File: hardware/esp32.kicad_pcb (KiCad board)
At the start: 4 copper layers, 60 x 40 mm, 86 parts, among them J101 USB-C-2, P101 EXT_HEADER, P201 CON-SENSOR2, P202 CON-SENSOR2, P203 CON-SENSOR2, P204 CON-SENSOR2, P205 CON-SENSOR2, P206 CON-SENSOR2, Q101 BC817, Q102 BC817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

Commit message: fix values
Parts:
- R108, R109: value 1k -> 2k2
- R110: value 470 -> 220

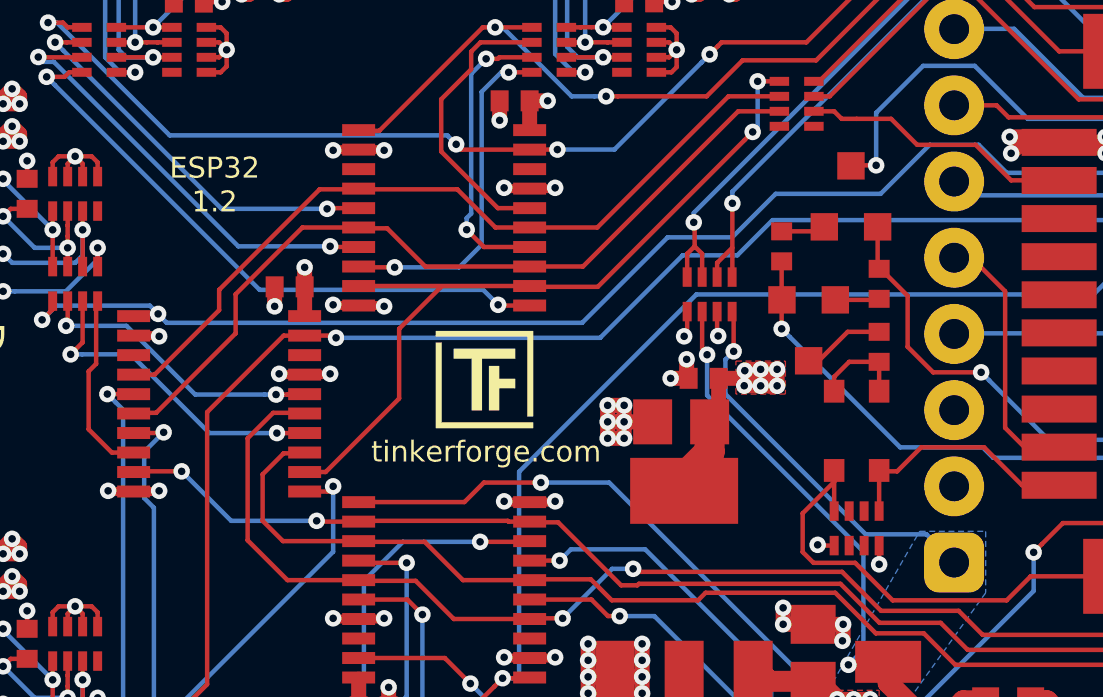
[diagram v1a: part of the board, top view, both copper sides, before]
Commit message: hardware version 1.3
 * fix reset logic
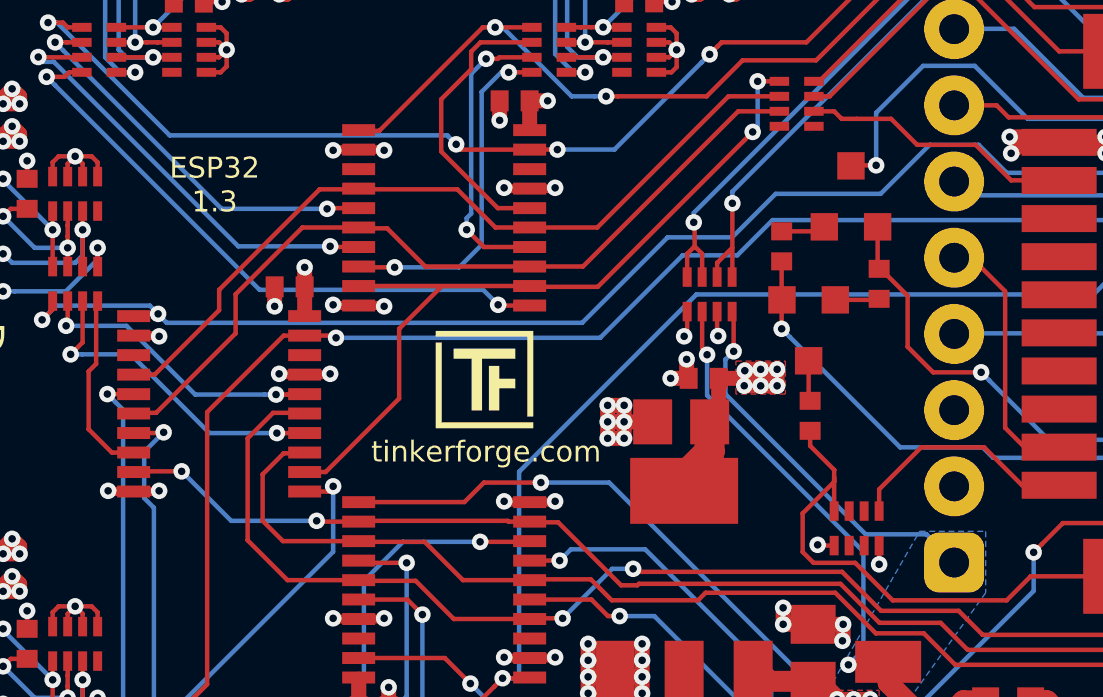
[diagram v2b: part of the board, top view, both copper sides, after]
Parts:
- removed D103, D104: BAT54HT1G, kicad-libraries:SOD-323
- C112: value DNP -> 10nF
- R108, R109: value 2k2 -> 12k
- R111: value 1k -> 10k
- moved R110 3.25 mm to (146.5, 144.1)
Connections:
- R110 pad 2: Net-(D103-Pad2) -> ESP_IO0
- RP103 pad 4: 3V3 -> GND
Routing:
- net Net-(D103-Pad2): track 3.11 -> 0.00 mm
- net ESP_IO0: track 15.1 -> 16.7 mm
- net Net-(Q102-PadC): track 2.74 -> 1.35 mm
- net GND: track 130.3 -> 130.9 mm, vias 135 -> 136
- net 3V3: track 52.0 -> 51.3 mm, vias 42 -> 41
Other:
- board text added: "ESP32 1.3"
- board text removed: "ESP32 1.2"

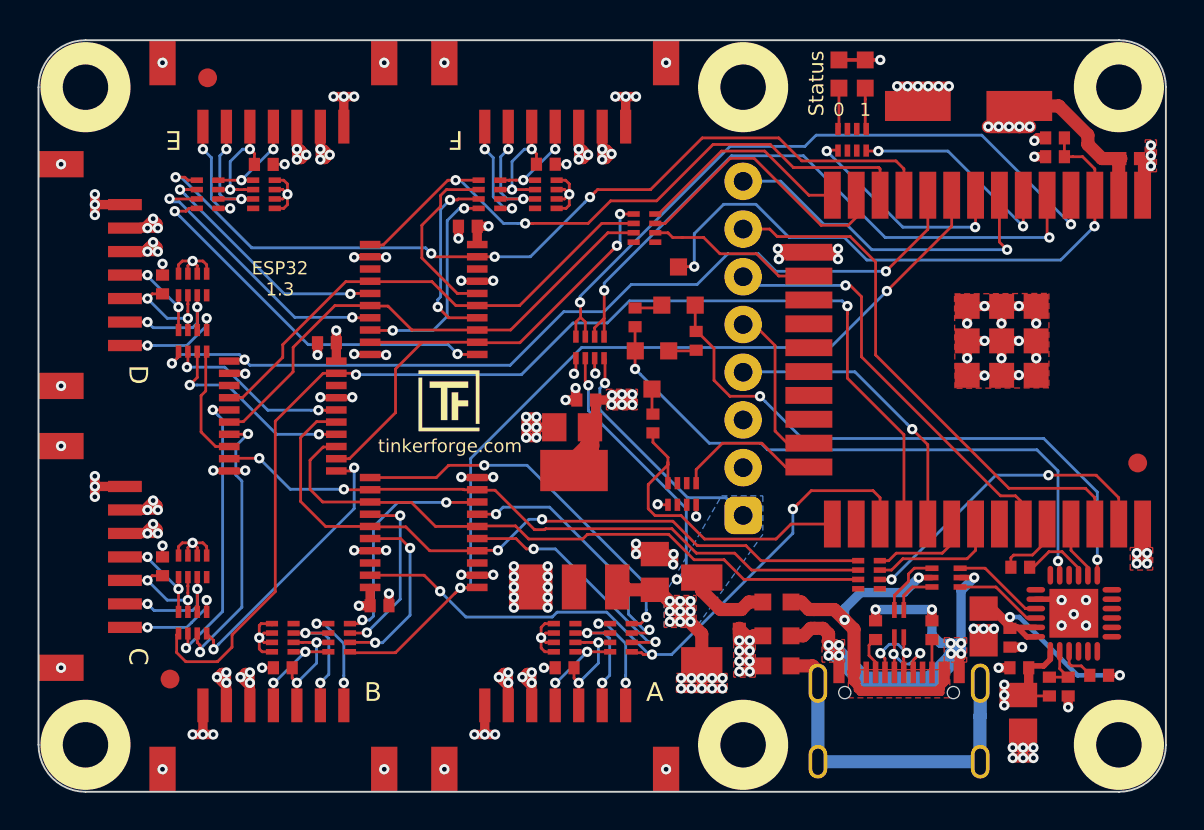
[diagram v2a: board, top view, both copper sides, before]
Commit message: add push buttons
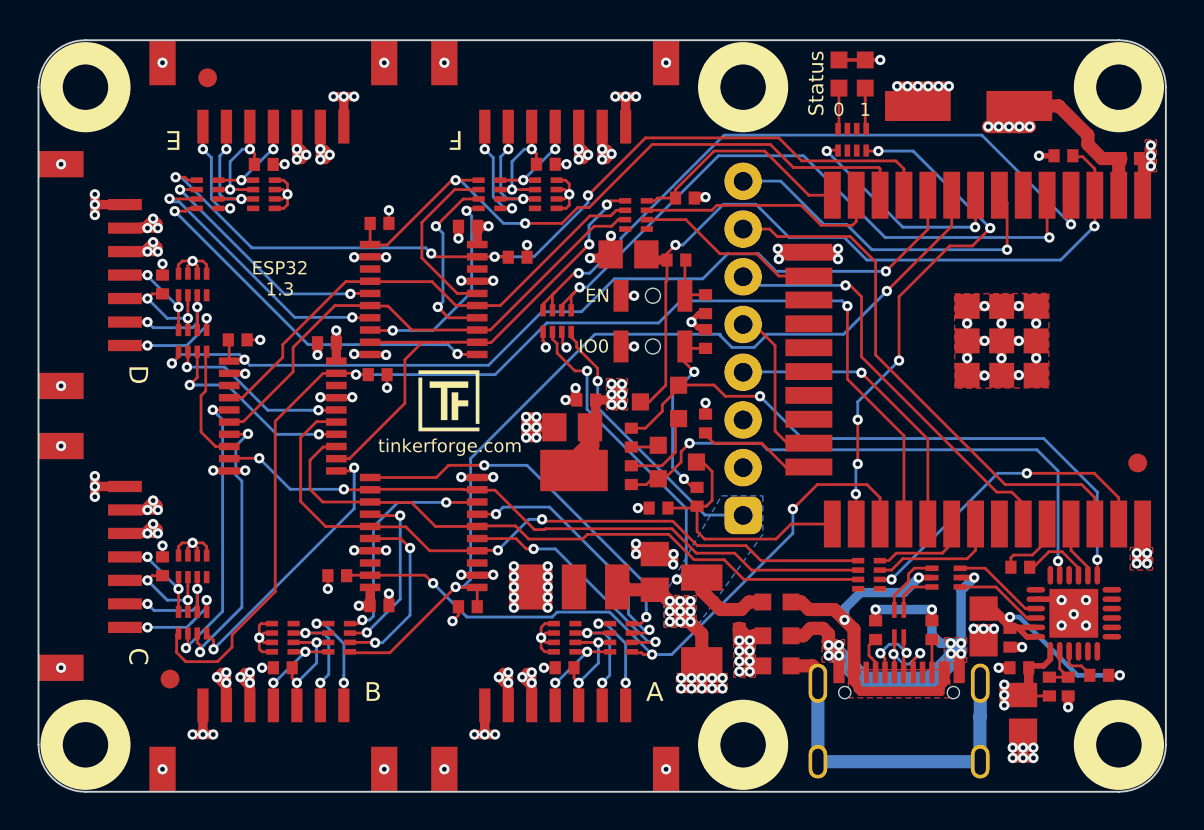
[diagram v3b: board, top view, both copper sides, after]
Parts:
- removed RP103: 1k, kicad-libraries:4X0402
- added C113: 1nF, kicad-libraries:C0402F, F.Cu at (149.3, 137.7)
- added C114: 1nF, kicad-libraries:C0402F, F.Cu at (149.3, 139.6)
- added R102: DNP/5k, kicad-libraries:R0402F, F.Cu at (148.2, 132.1)
- added R112: DNP/5k, kicad-libraries:R0402F, F.Cu at (149.3, 144.1)
- added R113: 470, kicad-libraries:R0402F, F.Cu at (147.8, 135.3)
- added R114: 470, kicad-libraries:R0402F, F.Cu at (148.8, 147.9)
- added R203: 10k, kicad-libraries:R0402F, F.Cu at (131.9, 133.4)
- added R204: 10k, kicad-libraries:R0402F, F.Cu at (124.4, 139.6)
- added R205: 10k, kicad-libraries:R0402F, F.Cu at (139.3, 135.2)
- added R206: 10k, kicad-libraries:R0402F, F.Cu at (131.8, 141.4)
- added R207: 10k, kicad-libraries:R0402F, F.Cu at (136.7, 153.8)
- added R208: 10k, kicad-libraries:R0402F, F.Cu at (129.7, 152.2)
- added SW101: B3U-1000P, kicad-libraries:B3U-1000P, F.Cu at (146.5, 137.2)
- added SW102: B3U-1000P, kicad-libraries:B3U-1000P, F.Cu at (146.5, 139.9)
- C112: value 10nF -> 10µF; footprint kicad-libraries:C0402F -> kicad-libraries:C0805E
- R110: value 220 -> DNP/5k
- R111: value 10k -> 12k
- moved C112 23.3 mm to (145.2, 135.1)
- moved R108 8.40 mm to (145.3, 146.8)
- moved Q101 6.25 mm to (146.8, 142.9), turned to 270 degrees
- moved R109 6.20 mm to (145.3, 144.8)
- moved Q102 5.08 mm to (147.8, 146.1), turned to 90 degrees
- moved R110 4.51 mm to (146.8, 148.6), turned to 180 degrees
- moved RP104 2.24 mm to (141.4, 138.6)
- moved R111 1.05 mm to (168.3, 129.8)
- moved RP101 0.83 mm to (145.6, 132.9)
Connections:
- net Net-(RP105-Pad5) renamed LED_BLUE
- Q102 pad C: Net-(Q102-PadC) -> ESP_IO0
- R110 pad 1: Net-(Q102-PadC) -> ESP_IO0
- R110 pad 2: ESP_IO0 -> 3V3
- RP105 pad 8: Net-(RP105-Pad8) -> LED_GREEN
- U104 pad 26: Net-(U104-Pad26) -> LED_GREEN
- U104 pad 6: Net-(RP105-Pad8) -> Net-(U104-Pad6)
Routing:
- net LED_GREEN: track 0.00 -> 27.7 mm, vias 0 -> 6
- net Net-(RP105-Pad8): track 11.7 -> 0.00 mm, vias 2 -> 0
- net Net-(C114-Pad1): track 0.00 -> 9.98 mm, vias 0 -> 2
- net ESP_EN: track 32.5 -> 40.2 mm
- net GND: track 130.9 -> 136.6 mm, vias 136 -> 141
- net 3V3: track 51.3 -> 55.4 mm, vias 41 -> 47
- net Net-(C113-Pad1): track 0.00 -> 3.64 mm
- net Net-(Q101-PadB): track 1.46 -> 4.51 mm
- net ESP_IO0: track 16.7 -> 14.2 mm
- net Net-(C101-Pad2): track 20.3 -> 22.8 mm
- net Net-(Q102-PadE): track 32.6 -> 30.2 mm
- net 5V: track 71.2 -> 73.1 mm
- net Net-(RP101-Pad7): track 15.0 -> 13.2 mm
- net B1-CS1: track 47.9 -> 49.7 mm
- net ESP_IO2: track 7.95 -> 6.31 mm
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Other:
- board text added: "EN"
- board text added: "IO0"
- board text added: "Input only"

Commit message: move push buttons
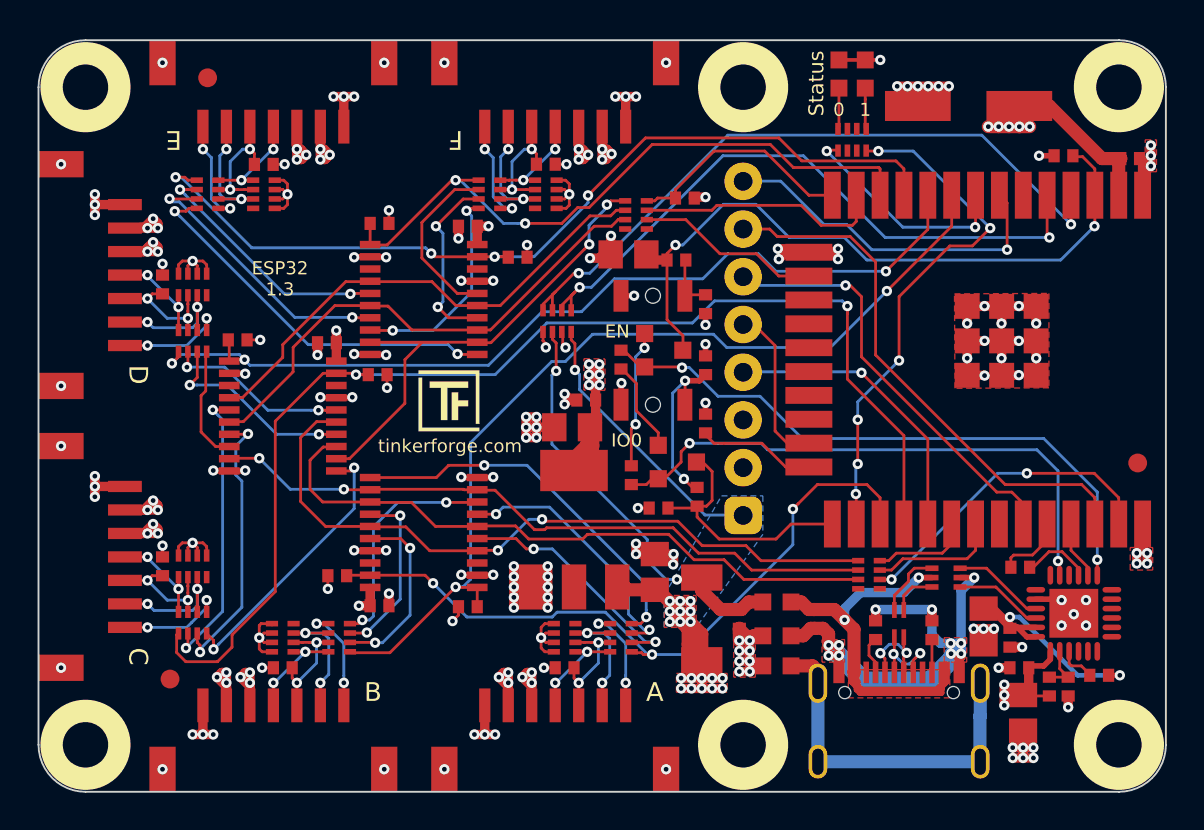
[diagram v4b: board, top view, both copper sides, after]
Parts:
- R102, R112: value DNP/5k -> DNP
- R110: value DNP/5k -> 5k
- R203, R204, R205, R206, R207, R208: value 10k -> DNP
- moved R109 4.19 mm to (144.8, 140.7)
- moved SW102 3.10 mm to (146.5, 143.1)
- moved Q101 2.76 mm to (147.1, 140.2), turned to 90 degrees
- moved C114 1.40 mm to (149.3, 140.9)
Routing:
- net Net-(Q102-PadB): track 1.49 -> 5.08 mm
- net ESP_EN: track 40.2 -> 37.0 mm
- net 5V: track 73.1 -> 76.0 mm
- net Net-(Q101-PadB): track 4.51 -> 7.31 mm, vias 0 -> 2
- net Net-(C114-Pad1): track 9.98 -> 9.15 mm
- net 3V3: track 55.4 -> 54.7 mm
- net GND: track 136.6 -> 136.2 mm, vias 141 -> 142

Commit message: Changed values of R108 and R109 from 12k to 100k Changed value of R110 form 5k to 12k
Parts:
- R108, R109: value 12k -> 100k
- R110: value 5k -> 12k
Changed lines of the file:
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@@
-(kicad_pcb (version 20171130) (host pcbnew 5.1.6-c6e7f7d~86~ubuntu18.04.1)
+(kicad_pcb (version 20171130) (host pcbnew "(5.1.4)-1")
   (general
     (thickness 1.6)
@@
   (layers
     (0 F.Cu signal)
-    (1 GND power hide)
-    (2 VCC power hide)
-    (31 B.Cu signal hide)
+    (1 GND power)
+    (2 VCC power)
+    (31 B.Cu signal)
     (32 B.Adhes user)
     (33 F.Adhes user)
@@
     (aux_axis_origin 113.8 123.65)
     (grid_origin 113.8 123.65)
-    (visible_elements FFFEFF7F)
+    (visible_elements 7FFFFFFF)
     (pcbplotparams
       (layerselection 0x010fc_ffffffff)
@@
       (effects (font (size 0.2 0.2) (thickness 0.05)))
     )
-    (fp_text value 12k (at 0 -0.15 90) (layer F.Fab)
+    (fp_text value 100k (at 0 -0.15 90) (layer F.Fab)
       (effects (font (size 0.2 0.2) (thickness 0.05)))
     )
@@
       (effects (font (size 0.2 0.2) (thickness 0.05)))
     )
-    (fp_text value 12k (at 0 -0.15 90) (layer F.Fab)
+    (fp_text value 100k (at 0 -0.15 90) (layer F.Fab)
       (effects (font (size 0.2 0.2) (thickness 0.05)))
     )
@@
       (effects (font (size 0.2 0.2) (thickness 0.05)))
     )
-    (fp_text value 5k (at 0 -0.15) (layer F.Fab)
+    (fp_text value 12k (at 0 -0.15) (layer F.Fab)
       (effects (font (size 0.2 0.2) (thickness 0.05)))
     )
